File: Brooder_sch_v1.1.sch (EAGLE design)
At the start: 37 parts, among them J2 1X2-3.5MM, J4 1X2-3.5MM, T1 2N2222, U1 328P

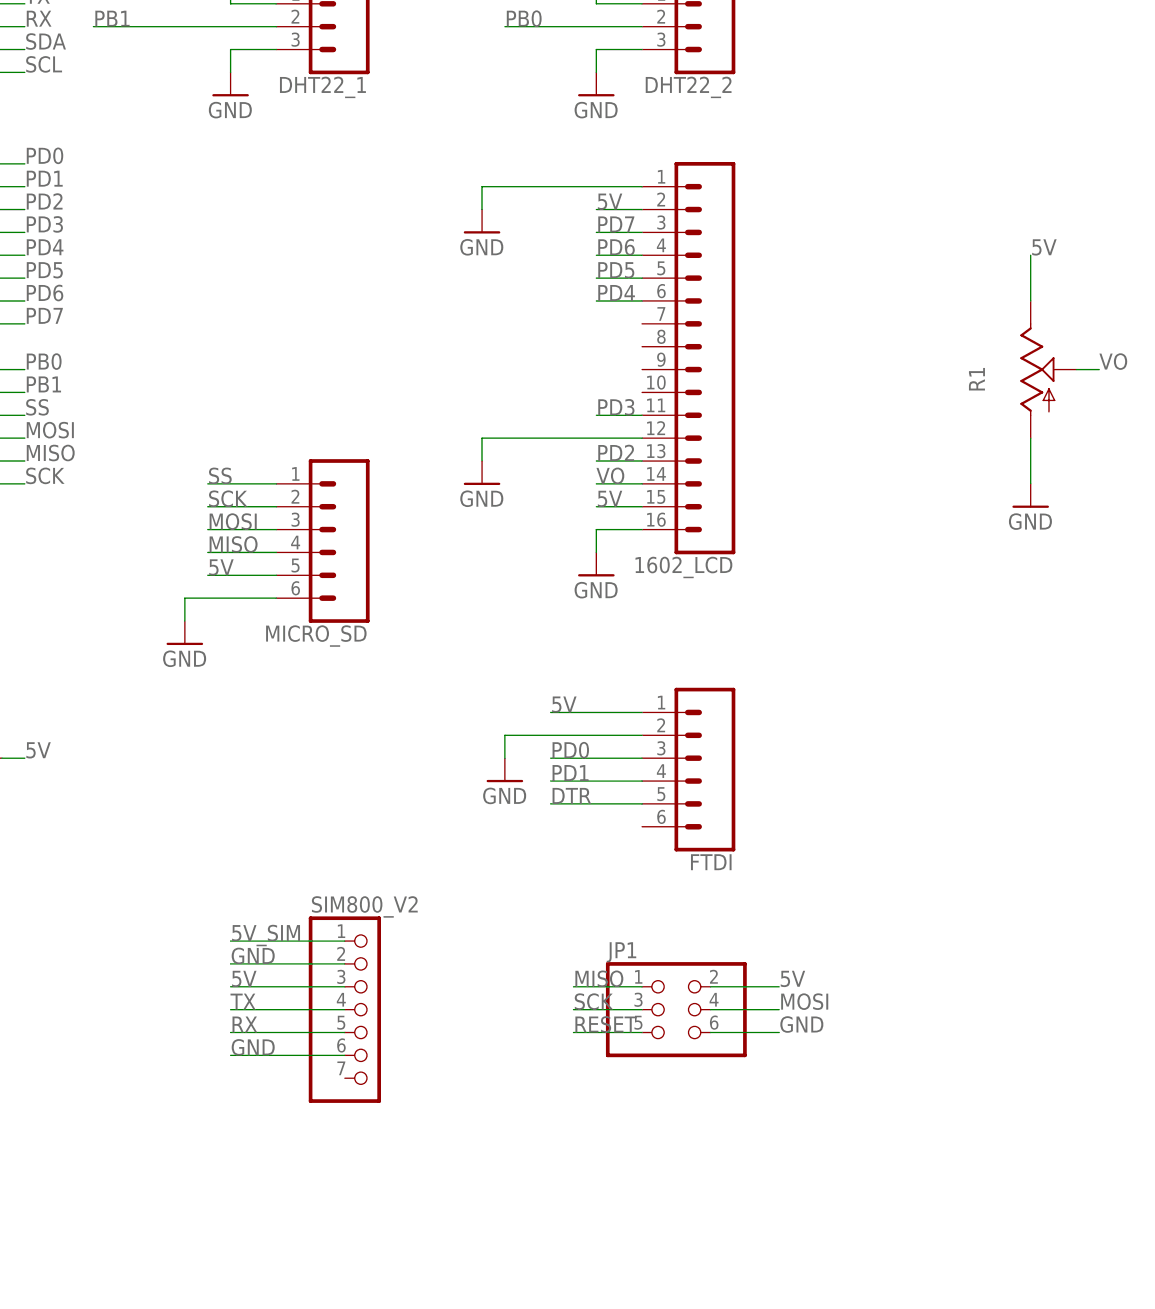
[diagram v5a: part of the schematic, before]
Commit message: Adds i2c header pin in place of lcd pins and potentiometer
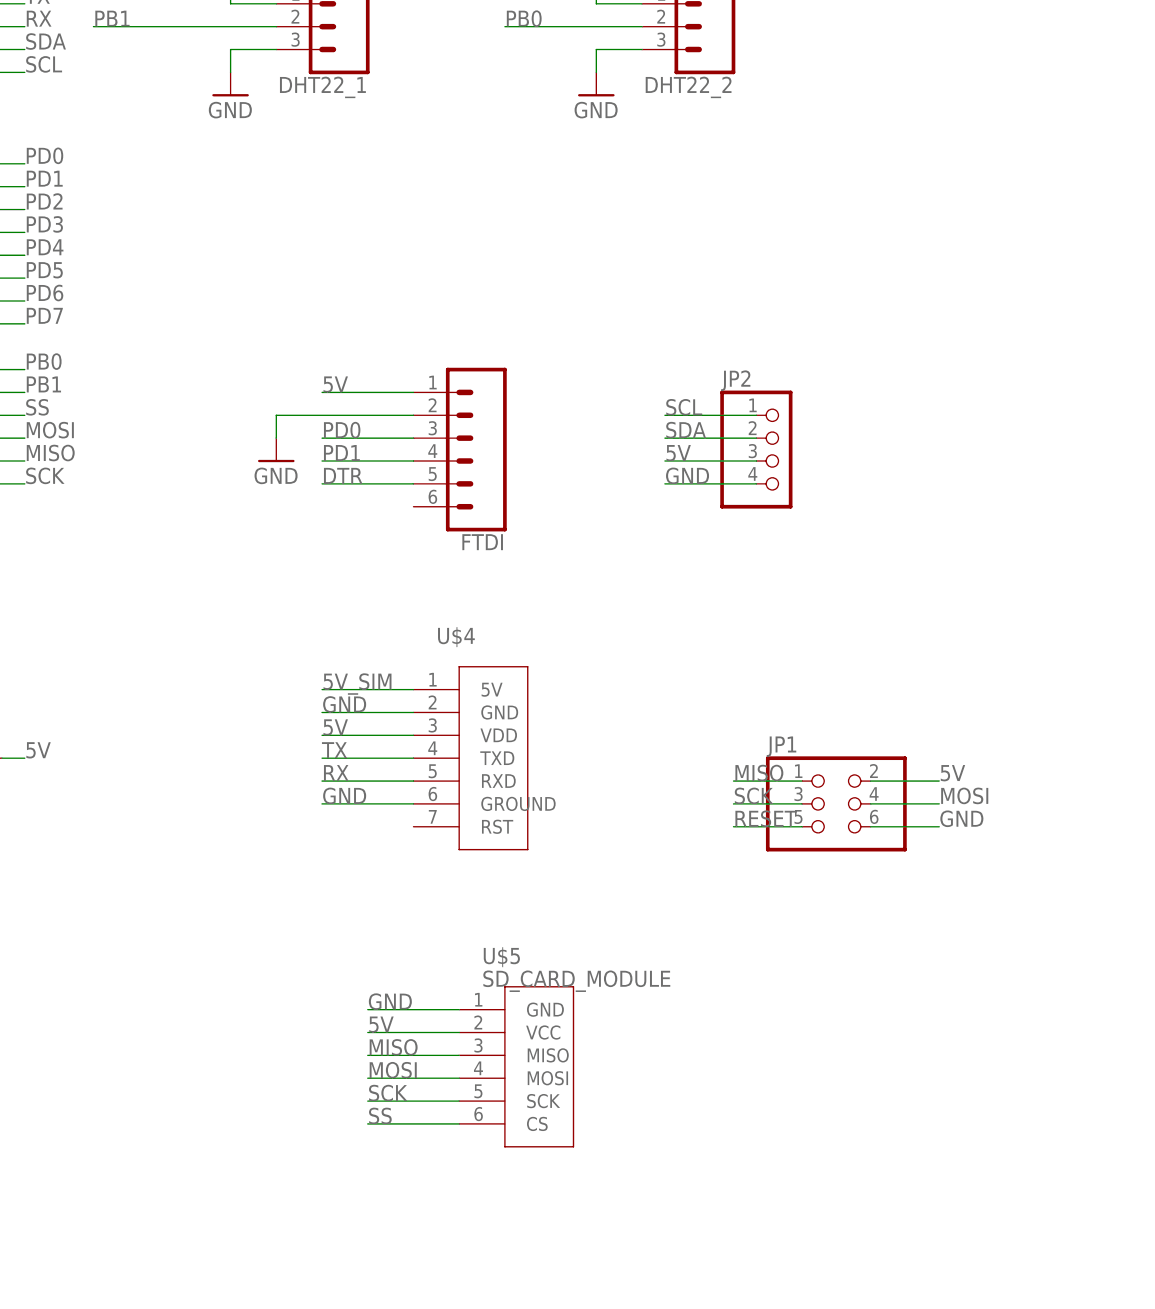
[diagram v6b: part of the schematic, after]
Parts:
- removed 1602_LCD: (no value), SparkFun-Connectors:CONN_161X16_NO_SILK
- removed MICRO_SD: (no value), SparkFun-Connectors:CONN_06NO_SILK_FEMALE_PTH
- removed R1: (no value), pot:TRIM_US-CT6
- removed SIM800_V2: (no value), pinhead:PINHD-1X7
- added JP2: (no value), pinhead:PINHD-1X4
- added U$4: (no value), custom_libraries:2004A
- added U$5: SD_CARD_MODULE, custom_libraries:SD_CARD_MODULE
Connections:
- removed net VO: 1602_LCD.14, R1.S
- net 5V: now also JP2.3, U$4.VDD, U$5.VCC; no longer 1602_LCD.15, 1602_LCD.2, MICRO_SD.5, R1.E, SIM800_V2.3
- net 5V_SIM: now also U$4.5V; no longer SIM800_V2.1
- net GND: now also JP2.4, U$4.GND, U$4.GROUND, U$5.GND; no longer 1602_LCD.1, 1602_LCD.12, 1602_LCD.16, MICRO_SD.6, R1.A, SIM800_V2.2, SIM800_V2.6
- net MISO: now also U$5.MISO; no longer MICRO_SD.4
- net MOSI: now also U$5.MOSI; no longer MICRO_SD.3
- net PD2: no longer 1602_LCD.13
- net PD3: no longer 1602_LCD.11
- net PD4: no longer 1602_LCD.6
- net PD5: no longer 1602_LCD.5
- net PD6: no longer 1602_LCD.4
- net PD7: no longer 1602_LCD.3
- net RX: now also U$4.RXD; no longer SIM800_V2.5
- net SCK: now also U$5.SCK; no longer MICRO_SD.2
- net SCL: now also JP2.1
- net SDA: now also JP2.2
- net SS: now also U$5.CS; no longer MICRO_SD.1
- net TX: now also U$4.TXD; no longer SIM800_V2.4
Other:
- moved on the sheet: FTDI, JP1

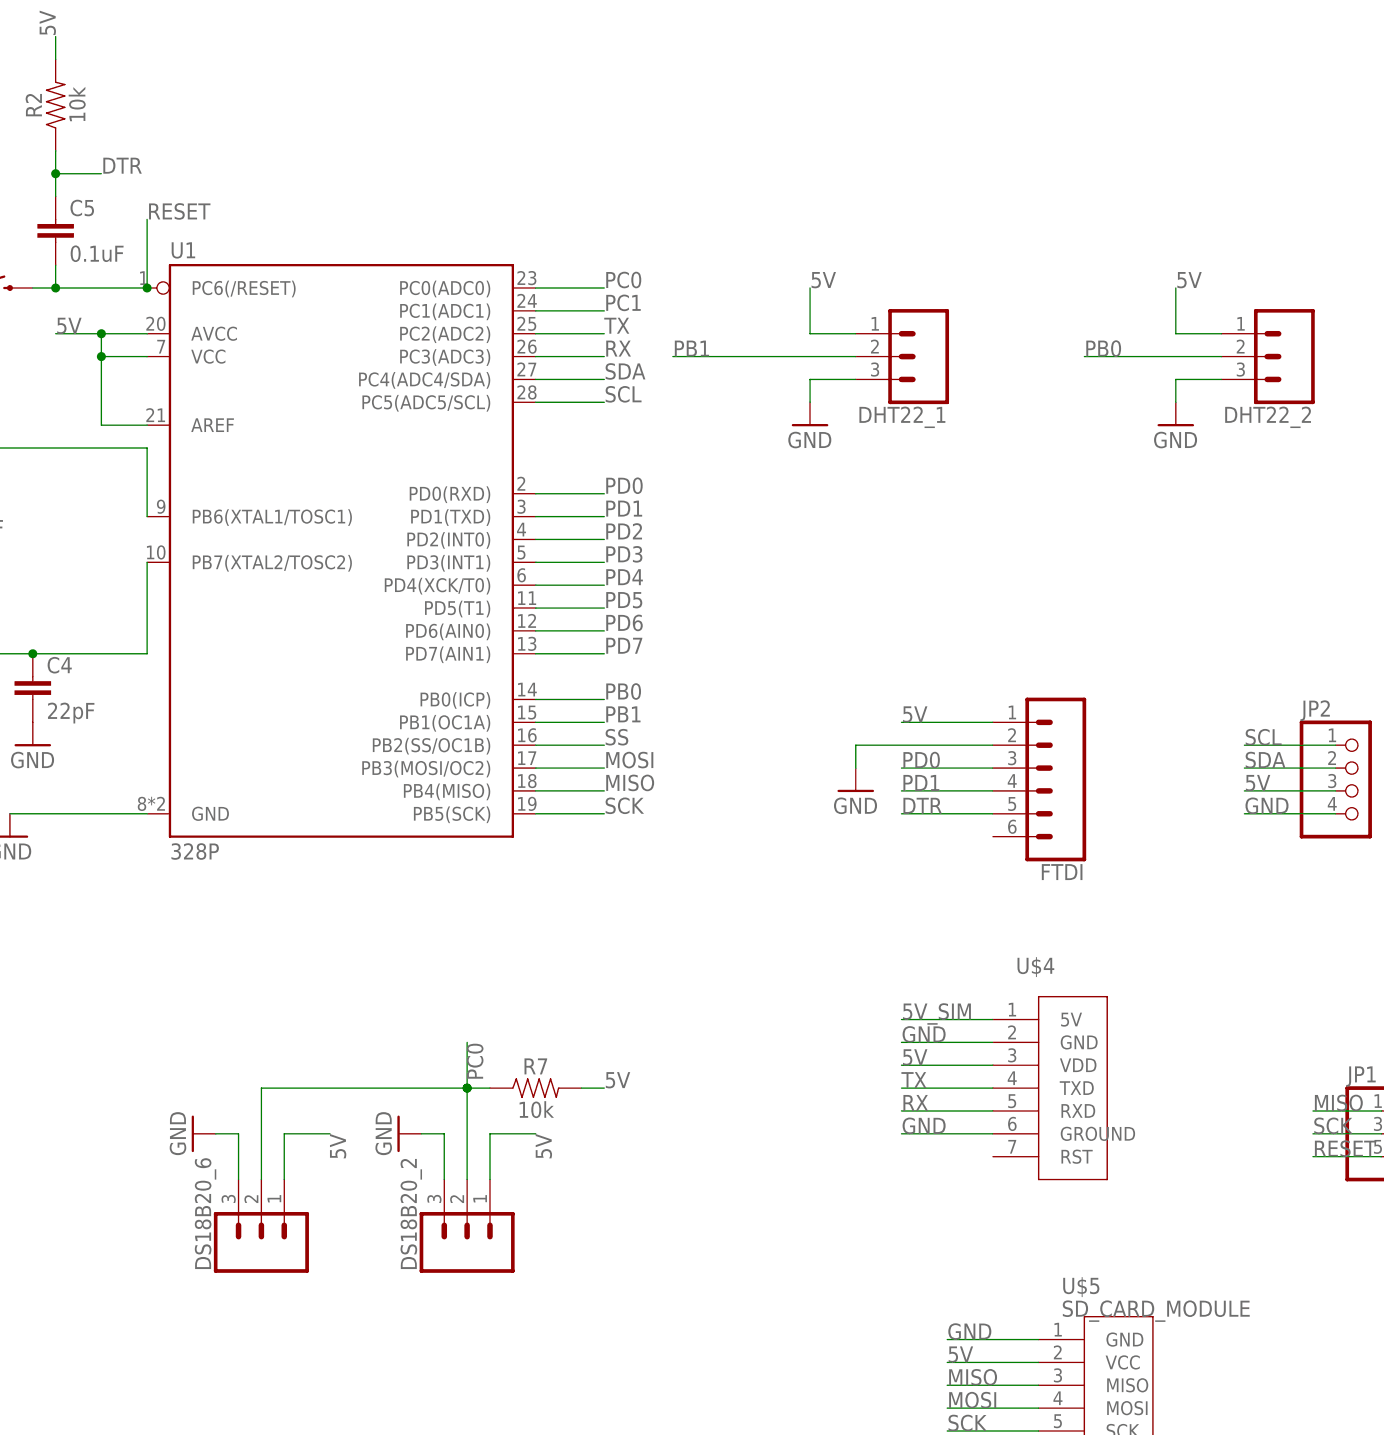
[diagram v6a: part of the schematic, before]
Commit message: Adds resitor to dht22(680)
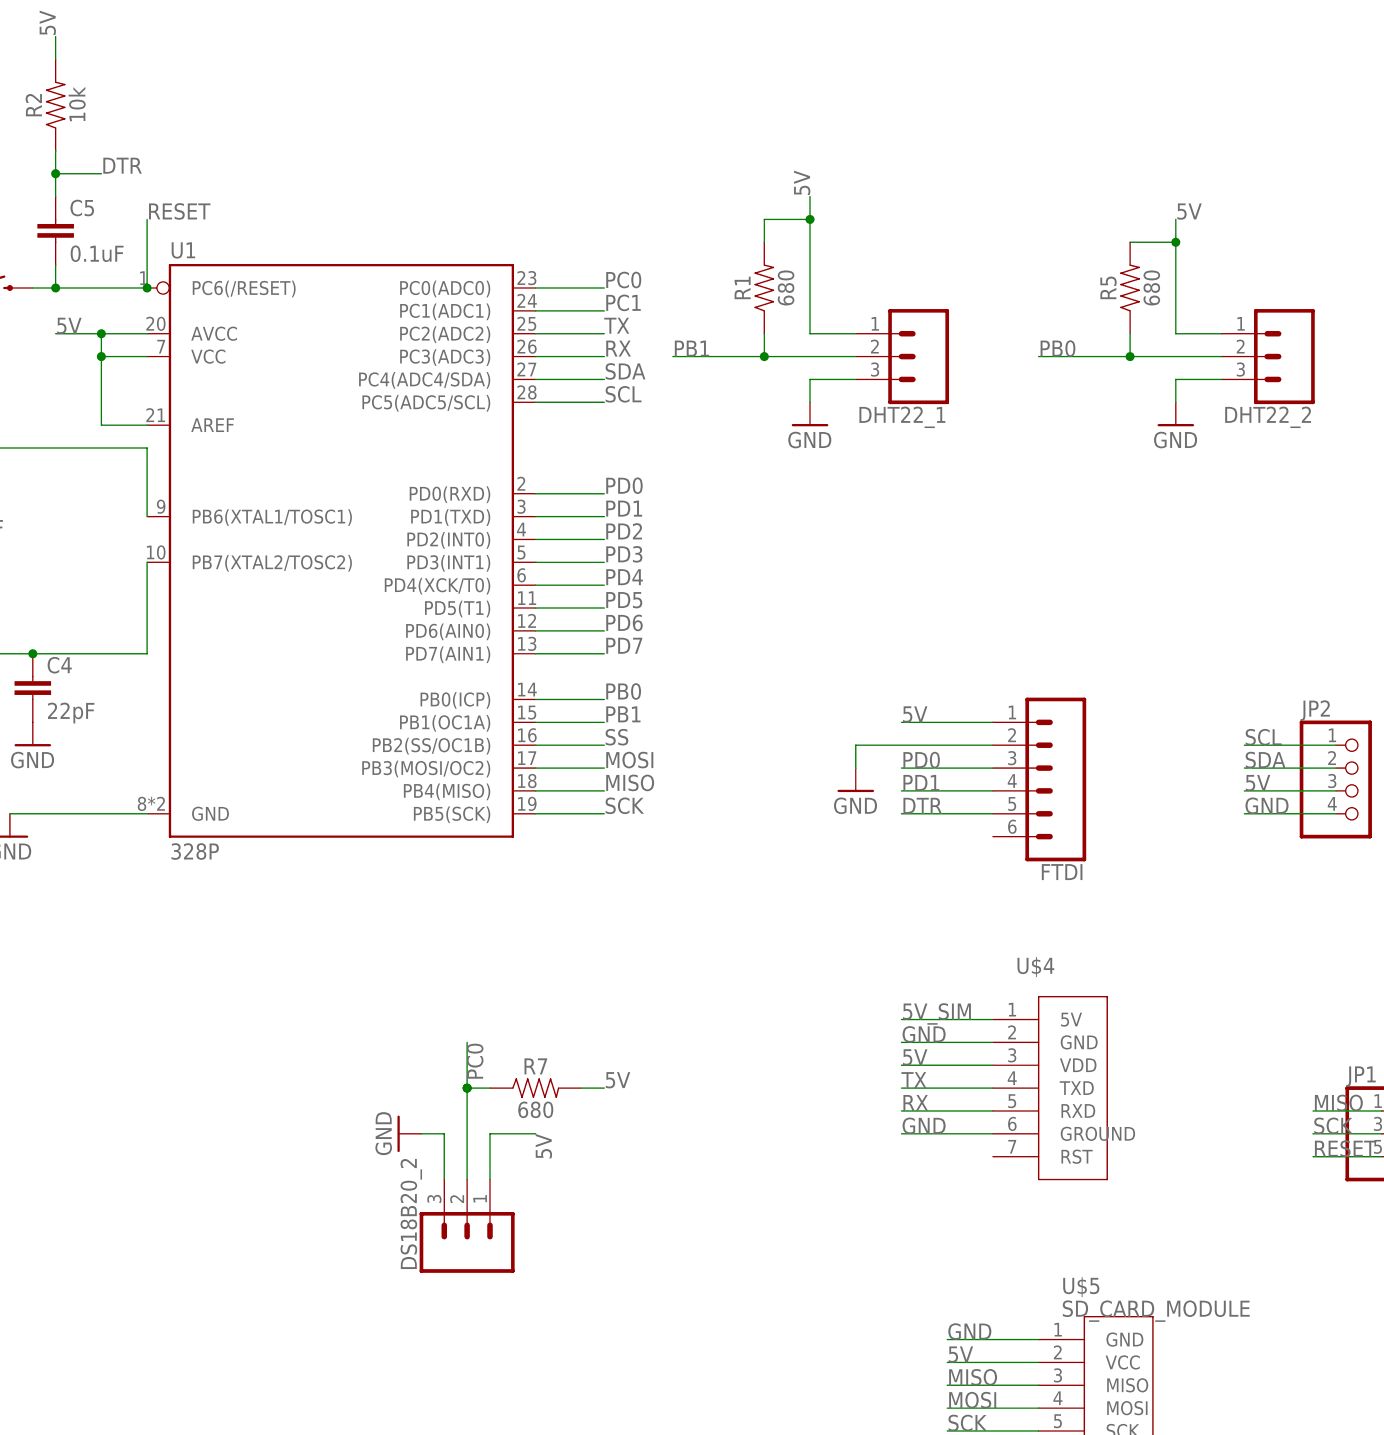
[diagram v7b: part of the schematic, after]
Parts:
- removed DS18B20_6: 455-1750-1-ND, SparkFun-Connectors:CONN_03
- added R1, R5: 680, SparkFun-Resistors:10MOHM-HORIZ-1/4W-5%
- R7: value 10k -> 680
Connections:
- net 5V: now also R1.2, R5.2; no longer DS18B20_6.1
- net GND: no longer DS18B20_6.3
- net PB0: now also R5.1
- net PB1: now also R1.1
- net PC0: no longer DS18B20_6.2
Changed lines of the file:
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@@
 <part name="DS18B20_2" library="SparkFun-Connectors" deviceset="CONN_03" device="" value="455-1750-1-ND"/>
 <part name="GND19" library="supply1" library_urn="urn:adsk.eagle:library:371" deviceset="GND" device=""/>
-<part name="R7" library="SparkFun-Resistors" deviceset="10MOHM" device="-HORIZ-1/4W-5%" value="10k"/>
-<part name="DS18B20_6" library="SparkFun-Connectors" deviceset="CONN_03" device="" value="455-1750-1-ND"/>
-<part name="GND23" library="supply1" library_urn="urn:adsk.eagle:library:371" deviceset="GND" device=""/>
+<part name="R7" library="SparkFun-Resistors" deviceset="10MOHM" device="-HORIZ-1/4W-5%" value="680"/>
 <part name="GND18" library="supply1" library_urn="urn:adsk.eagle:library:371" deviceset="GND" device=""/>
 <part name="J2" library="adafruit" deviceset="1X2" device="-3.5MM"/>
@@
 <part name="U$5" library="custom_libraries" deviceset="SD_CARD_MODULE" device=""/>
 <part name="JP2" library="pinhead" deviceset="PINHD-1X4" device=""/>
+<part name="R1" library="SparkFun-Resistors" deviceset="10MOHM" device="-HORIZ-1/4W-5%" value="680"/>
+<part name="R5" library="SparkFun-Resistors" deviceset="10MOHM" device="-HORIZ-1/4W-5%" value="680"/>
 </parts>
 <sheets>
@@
 <attribute name="VALUE" x="76.2" y="13.716" size="1.778" layer="96" font="vector" align="top-center"/>
 </instance>
-<instance part="DS18B20_6" gate="J$1" x="45.72" y="-2.54" smashed="yes" rot="R90">
-<attribute name="NAME" x="40.132" y="-5.08" size="1.778" layer="95" font="vector" rot="R90"/>
-</instance>
-<instance part="GND23" gate="1" x="38.1" y="10.16" smashed="yes" rot="R270">
-<attribute name="VALUE" x="35.56" y="12.7" size="1.778" layer="96" rot="R270"/>
-</instance>
 <instance part="GND18" gate="1" x="111.76" y="48.26" smashed="yes">
 <attribute name="VALUE" x="109.22" y="45.72" size="1.778" layer="96"/>
@@
 <instance part="U$5" gate="G$1" x="160.02" y="-12.7"/>
 <instance part="JP2" gate="A" x="167.64" y="48.26"/>
+<instance part="R1" gate="G$1" x="101.6" y="104.14" smashed="yes" rot="R90">
+<attribute name="NAME" x="100.076" y="104.14" size="1.778" layer="95" font="vector" rot="R90" align="bottom-center"/>
+<attribute name="VALUE" x="103.124" y="104.14" size="1.778" layer="96" font="vector" rot="R90" align="top-center"/>
+</instance>
+<instance part="R5" gate="G$1" x="142.24" y="104.14" smashed="yes" rot="R90">
+<attribute name="NAME" x="140.716" y="104.14" size="1.778" layer="95" font="vector" rot="R90" align="bottom-center"/>
+<attribute name="VALUE" x="143.764" y="104.14" size="1.778" layer="96" font="vector" rot="R90" align="top-center"/>
+</instance>
 </instances>
 <busses>
@@
 <wire x1="66.04" y1="10.16" x2="63.5" y2="10.16" width="0.1524" layer="91"/>
 <pinref part="GND19" gate="1" pin="GND"/>
-</segment>
-<segment>
-<pinref part="DS18B20_6" gate="J$1" pin="3"/>
-<wire x1="43.18" y1="5.08" x2="43.18" y2="10.16" width="0.1524" layer="91"/>
-<wire x1="43.18" y1="10.16" x2="40.64" y2="10.16" width="0.1524" layer="91"/>
-<pinref part="GND23" gate="1" pin="GND"/>
 </segment>
 <segment>
@@
 <pinref part="DHT22_1" gate="J$1" pin="1"/>
 <wire x1="111.76" y1="99.06" x2="106.68" y2="99.06" width="0.1524" layer="91"/>
-<wire x1="106.68" y1="99.06" x2="106.68" y2="104.14" width="0.1524" layer="91"/>
-<label x="106.68" y="104.14" size="1.778" layer="95"/>
+<wire x1="106.68" y1="99.06" x2="106.68" y2="111.76" width="0.1524" layer="91"/>
+<label x="106.68" y="114.3" size="1.778" layer="95" rot="R90"/>
+<pinref part="R1" gate="G$1" pin="2"/>
+<wire x1="106.68" y1="111.76" x2="106.68" y2="114.3" width="0.1524" layer="91"/>
+<wire x1="101.6" y1="109.22" x2="101.6" y2="111.76" width="0.1524" layer="91"/>
+<wire x1="101.6" y1="111.76" x2="106.68" y2="111.76" width="0.1524" layer="91"/>
+<junction x="106.68" y="111.76"/>
 </segment>
 <segment>
 <pinref part="DHT22_2" gate="J$1" pin="1"/>
 <wire x1="152.4" y1="99.06" x2="147.32" y2="99.06" width="0.1524" layer="91"/>
-<wire x1="147.32" y1="99.06" x2="147.32" y2="104.14" width="0.1524" layer="91"/>
-<label x="147.32" y="104.14" size="1.778" layer="95"/>
+<wire x1="147.32" y1="99.06" x2="147.32" y2="109.22" width="0.1524" layer="91"/>
+<label x="147.32" y="111.76" size="1.778" layer="95"/>
+<pinref part="R5" gate="G$1" pin="2"/>
+<wire x1="147.32" y1="109.22" x2="147.32" y2="111.76" width="0.1524" layer="91"/>
+<wire x1="142.24" y1="109.22" x2="147.32" y2="109.22" width="0.1524" layer="91"/>
+<junction x="147.32" y="109.22"/>
 </segment>
 <segment>
@@
 <wire x1="81.28" y1="15.24" x2="83.82" y2="15.24" width="0.1524" layer="91"/>
 <label x="83.82" y="15.24" size="1.778" layer="95"/>
-</segment>
-<segment>
-<pinref part="DS18B20_6" gate="J$1" pin="1"/>
-<wire x1="48.26" y1="5.08" x2="48.26" y2="10.16" width="0.1524" layer="91"/>
-<wire x1="48.26" y1="10.16" x2="53.34" y2="10.16" width="0.1524" layer="91"/>
-<label x="53.34" y="10.16" size="1.778" layer="95" rot="R270"/>
 </segment>
 <segment>
@@
 <segment>
 <pinref part="DHT22_2" gate="J$1" pin="2"/>
-<wire x1="152.4" y1="96.52" x2="137.16" y2="96.52" width="0.1524" layer="91"/>
-<label x="137.16" y="96.52" size="1.778" layer="95"/>
+<wire x1="152.4" y1="96.52" x2="142.24" y2="96.52" width="0.1524" layer="91"/>
+<label x="132.08" y="96.52" size="1.778" layer="95"/>
+<pinref part="R5" gate="G$1" pin="1"/>
+<wire x1="142.24" y1="96.52" x2="132.08" y2="96.52" width="0.1524" layer="91"/>
+<wire x1="142.24" y1="99.06" x2="142.24" y2="96.52" width="0.1524" layer="91"/>
+<junction x="142.24" y="96.52"/>
 </segment>
 </net>
@@
 <segment>
 <pinref part="DHT22_1" gate="J$1" pin="2"/>
-<wire x1="111.76" y1="96.52" x2="91.44" y2="96.52" width="0.1524" layer="91"/>
+<wire x1="111.76" y1="96.52" x2="101.6" y2="96.52" width="0.1524" layer="91"/>
 <label x="91.44" y="96.52" size="1.778" layer="95"/>
+<pinref part="R1" gate="G$1" pin="1"/>
+<wire x1="101.6" y1="96.52" x2="91.44" y2="96.52" width="0.1524" layer="91"/>
+<wire x1="101.6" y1="99.06" x2="101.6" y2="96.52" width="0.1524" layer="91"/>
+<junction x="101.6" y="96.52"/>
 </segment>
 </net>
@@
 <wire x1="68.58" y1="5.08" x2="68.58" y2="15.24" width="0.1524" layer="91"/>
 <junction x="68.58" y="15.24"/>
-<wire x1="45.72" y1="15.24" x2="68.58" y2="15.24" width="0.1524" layer="91"/>
-<pinref part="DS18B20_6" gate="J$1" pin="2"/>
-<wire x1="45.72" y1="5.08" x2="45.72" y2="15.24" width="0.1524" layer="91"/>
-</segment>
-</net>
+</segment>
+</net>
